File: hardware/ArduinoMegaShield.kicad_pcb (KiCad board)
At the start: 2 copper layers, 30 parts, among them P1 CONN_01X02, P10 CONN_01X02, P11 CONN_01X02, P12 CONN_01X02, P13 CONN_01X02, P14 CONN_01X02, P15 CONN_01X02, P16 CONN_01X02, P2 CONN_01X02, P3 CONN_01X02, P4 CONN_01X02, P5 CONN_01X02, P6 CONN_01X02, P7 CONN_01X02, P8 CONN_01X02, P9 CONN_01X02

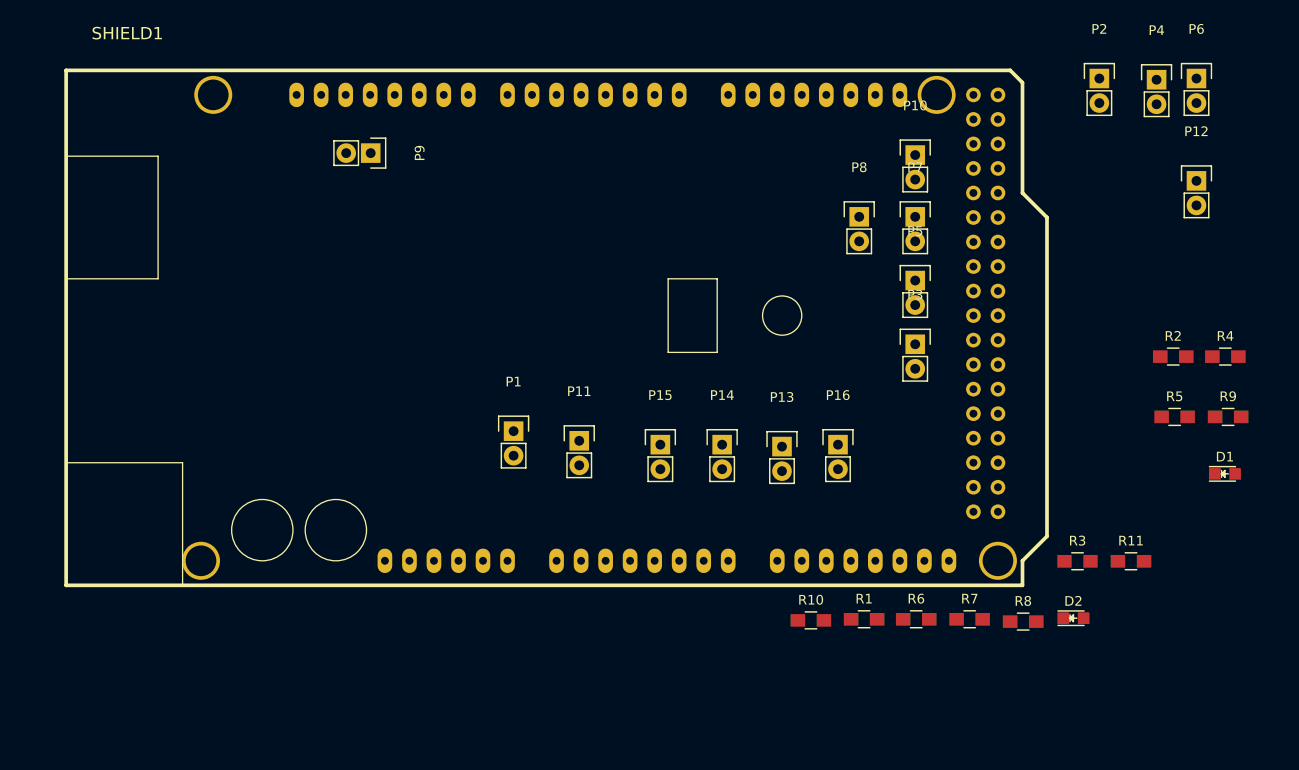
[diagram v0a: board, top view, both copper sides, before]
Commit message: changed terminal connectors from dupont to 200 mil screw terminals
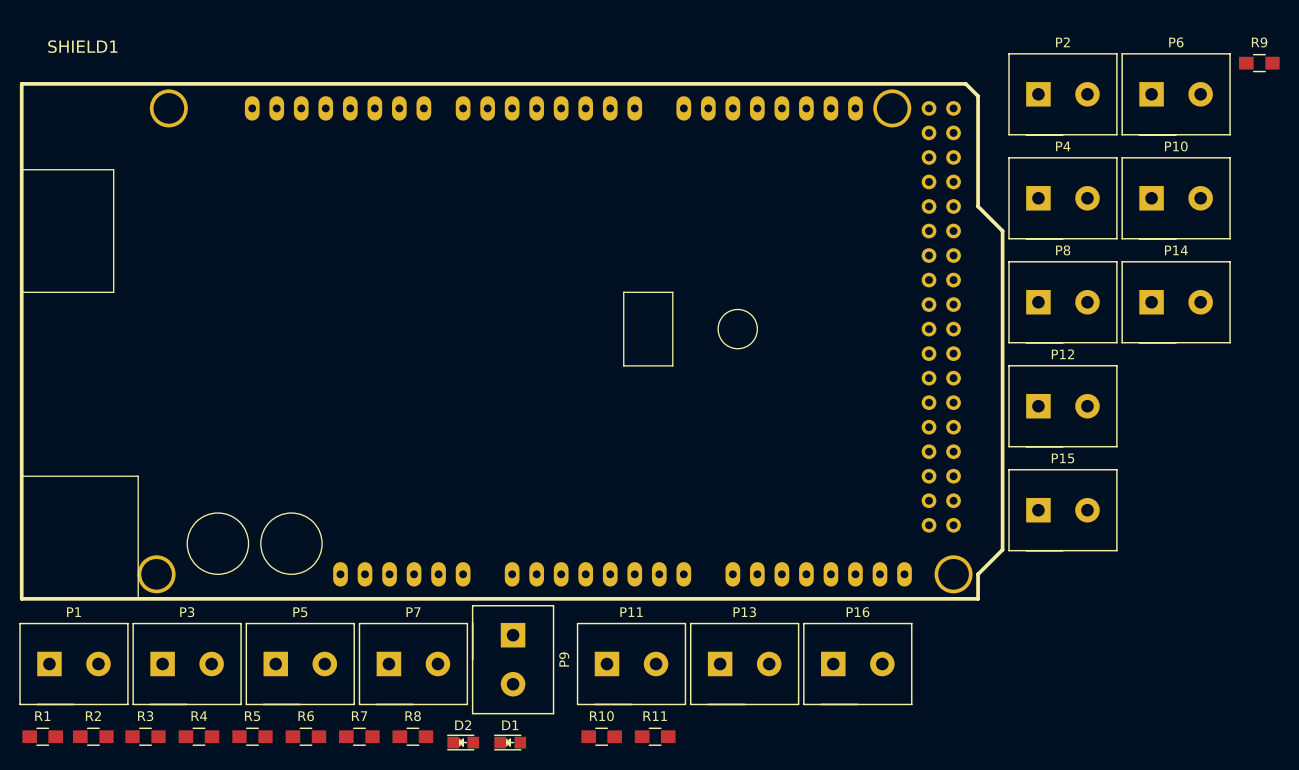
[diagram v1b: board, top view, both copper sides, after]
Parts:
- removed the P4 at (209.4, 72.0)
- added P2: CONN_01X02, 6axis:Terminal_Block_200_mil, F.Cu at (199.7, 73.5)
- P1, P10, P11, P12, P13, P14, P15, P16, P3, P5, P6, P7, P8, P9: footprint Pin_Headers:Pin_Header_Straight_1x02 -> 6axis:Terminal_Block_200_mil
- P4: renamed from P2; footprint Pin_Headers:Pin_Header_Straight_1x02 -> 6axis:Terminal_Block_200_mil
- moved R2 118.6 mm to (99.3, 140.1)
- moved R4 113.4 mm to (110.2, 140.1)
- moved R5 101.1 mm to (115.8, 140.1)
- moved R3 98.2 mm to (104.7, 140.1)
- moved R1 85.9 mm to (94.0, 140.1)
- moved P3 82.4 mm to (109.0, 132.5)
- moved D1 79.1 mm to (142.4, 140.7)
- moved P5 75.1 mm to (120.7, 132.5)
- moved P7 69.6 mm to (132.4, 132.5)
- moved D2 64.5 mm to (137.6, 140.7)
- moved R6 64.4 mm to (121.3, 140.1)
- moved R7 64.4 mm to (126.8, 140.1)
- moved R8 64.3 mm to (132.4, 140.1)
- moved P9 54.5 mm to (142.7, 132.1)
- moved R11 52.5 mm to (157.5, 140.1)
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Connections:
- P4 pad 1: /Z-Dir -> +5V
- P4 pad 2: GND -> /~ENABLE

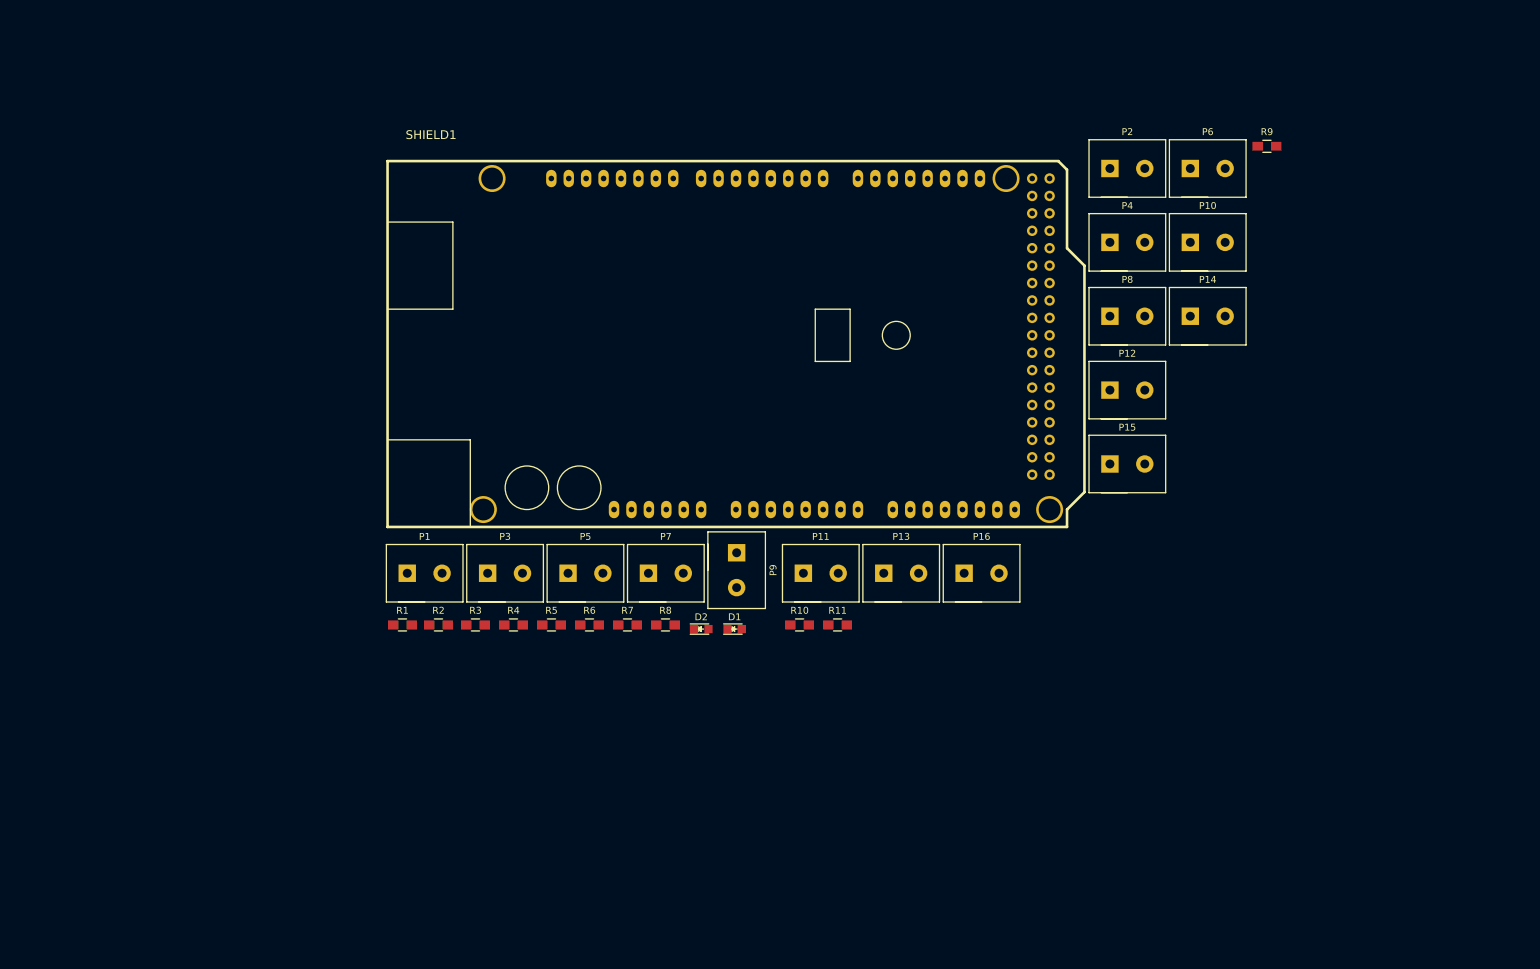
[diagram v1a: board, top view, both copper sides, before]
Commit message: added footprints for caps and motor drivers
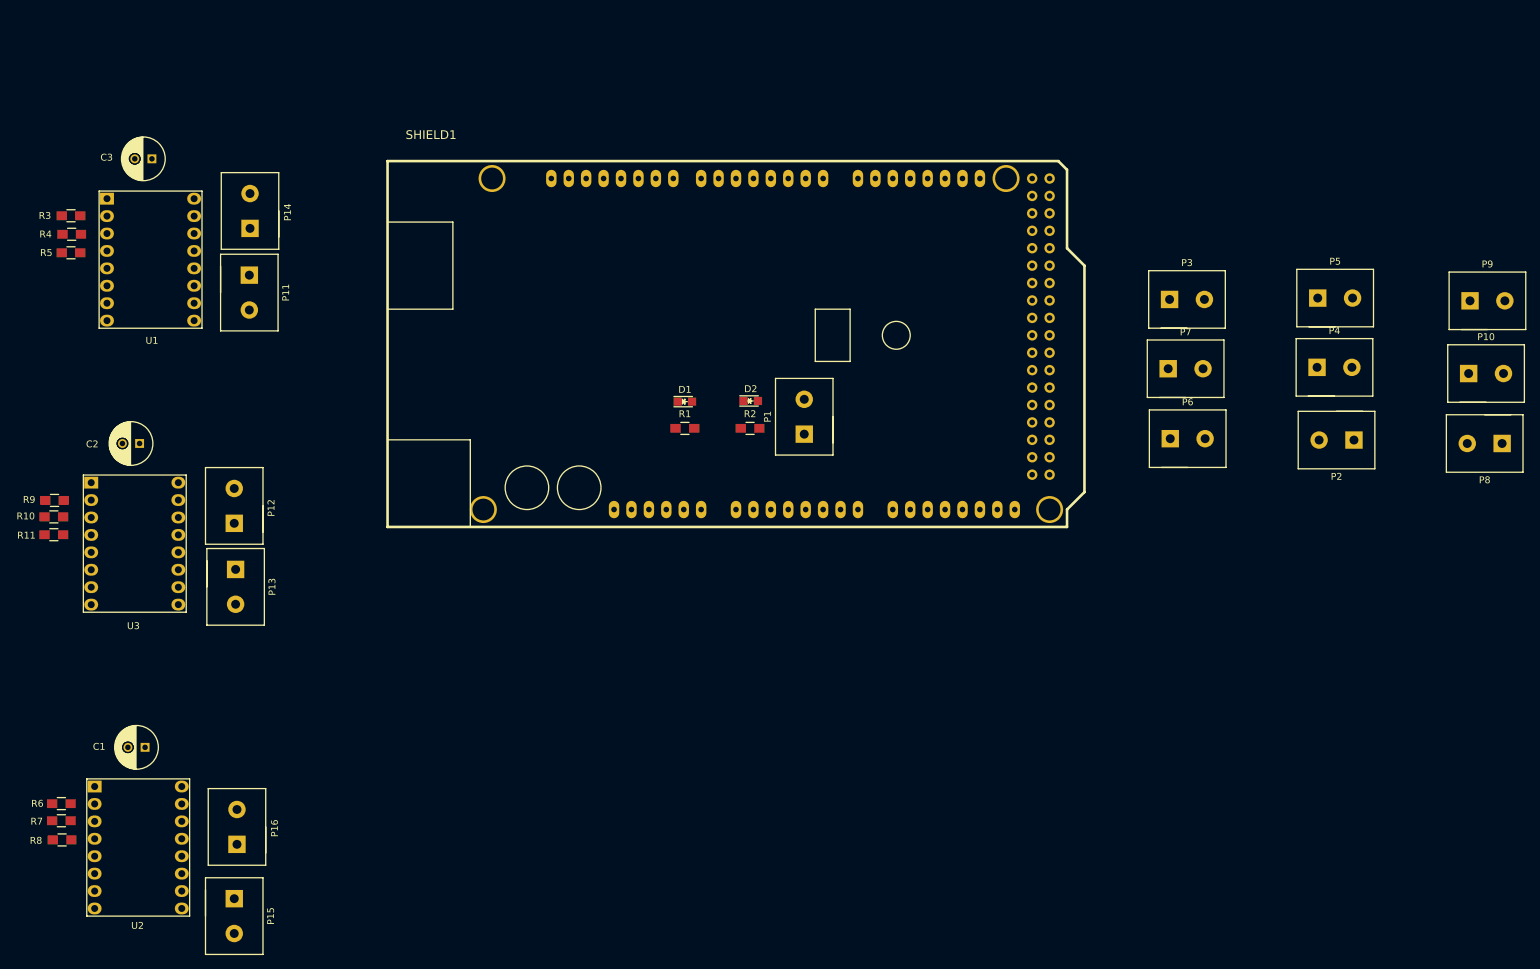
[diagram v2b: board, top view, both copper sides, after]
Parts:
- added C1: 100u, Capacitors_THT:C_Radial_D6.3_L11.2_P2.5, F.Cu at (56.5, 157.9)
- added C2: 100u, Capacitors_THT:C_Radial_D6.3_L11.2_P2.5, F.Cu at (55.7, 113.6)
- added C3: 100u, Capacitors_THT:C_Radial_D6.3_L11.2_P2.5, F.Cu at (57.5, 72.1)
- added U1: A4988, 6axis:A4988, F.Cu at (57.3, 86.8)
- added U2: A4988, 6axis:A4988, F.Cu at (55.5, 172.5)
- added U3: A4988, 6axis:A4988, F.Cu at (55.0, 128.2)
- moved R9 184.1 mm to (43.3, 121.9), turned to 180 degrees
- moved P15 145.9 mm to (69.5, 182.5), turned to 270 degrees
- moved P14 140.5 mm to (71.8, 79.7), turned to 90 degrees
- moved P12 131.3 mm to (69.5, 122.7), turned to 90 degrees
- moved P5 116.4 mm to (230.0, 92.4)
- moved P9 116.3 mm to (252.2, 92.8), turned to 0 degrees
- moved R11 115.0 mm to (43.2, 126.9), turned to 180 degrees
- moved P16 114.7 mm to (69.9, 169.5), turned to 90 degrees
- moved R10 109.9 mm to (43.2, 124.3), turned to 180 degrees
- moved P3 107.1 mm to (208.4, 92.6)
- moved P13 97.1 mm to (69.7, 134.5), turned to 270 degrees
- moved R8 93.4 mm to (44.4, 171.4), turned to 180 degrees
- moved P11 92.8 mm to (71.7, 91.6), turned to 270 degrees
- moved R5 88.6 mm to (45.7, 85.8), turned to 180 degrees
- moved R7 87.3 mm to (44.3, 168.6), turned to 180 degrees
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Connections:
- P11 pad 1: (no net) -> /A1A
- P11 pad 2: (no net) -> /A1B
- P12 pad 1: (no net) -> /C2A
- P12 pad 2: (no net) -> /C2B
- P13 pad 1: (no net) -> /C1A
- P13 pad 2: (no net) -> /C1B
- P14 pad 1: (no net) -> /A2A
- P14 pad 2: (no net) -> /A2B
- P15 pad 1: (no net) -> /B1A
- P15 pad 2: (no net) -> /B1B
- P16 pad 1: (no net) -> /B2A
- P16 pad 2: (no net) -> /B2B
- R10 pad 1: (no net) -> Net-(R10-Pad1)
- R11 pad 1: (no net) -> Net-(R11-Pad1)
- R3 pad 1: (no net) -> Net-(R3-Pad1)
- R4 pad 1: (no net) -> Net-(R4-Pad1)
- R5 pad 1: (no net) -> Net-(R5-Pad1)
- R6 pad 1: (no net) -> Net-(R6-Pad1)
- R7 pad 1: (no net) -> Net-(R7-Pad1)
- R8 pad 1: (no net) -> Net-(R8-Pad1)
- R9 pad 1: (no net) -> Net-(R9-Pad1)
- SHIELD1 pad 27: (no net) -> /A-Step
- SHIELD1 pad 28: (no net) -> /B-Step
- SHIELD1 pad 29: (no net) -> /C-Step
- SHIELD1 pad 33: (no net) -> /A-Dir
- SHIELD1 pad 34: (no net) -> /B-Dir
- SHIELD1 pad 35: (no net) -> /C-Dir

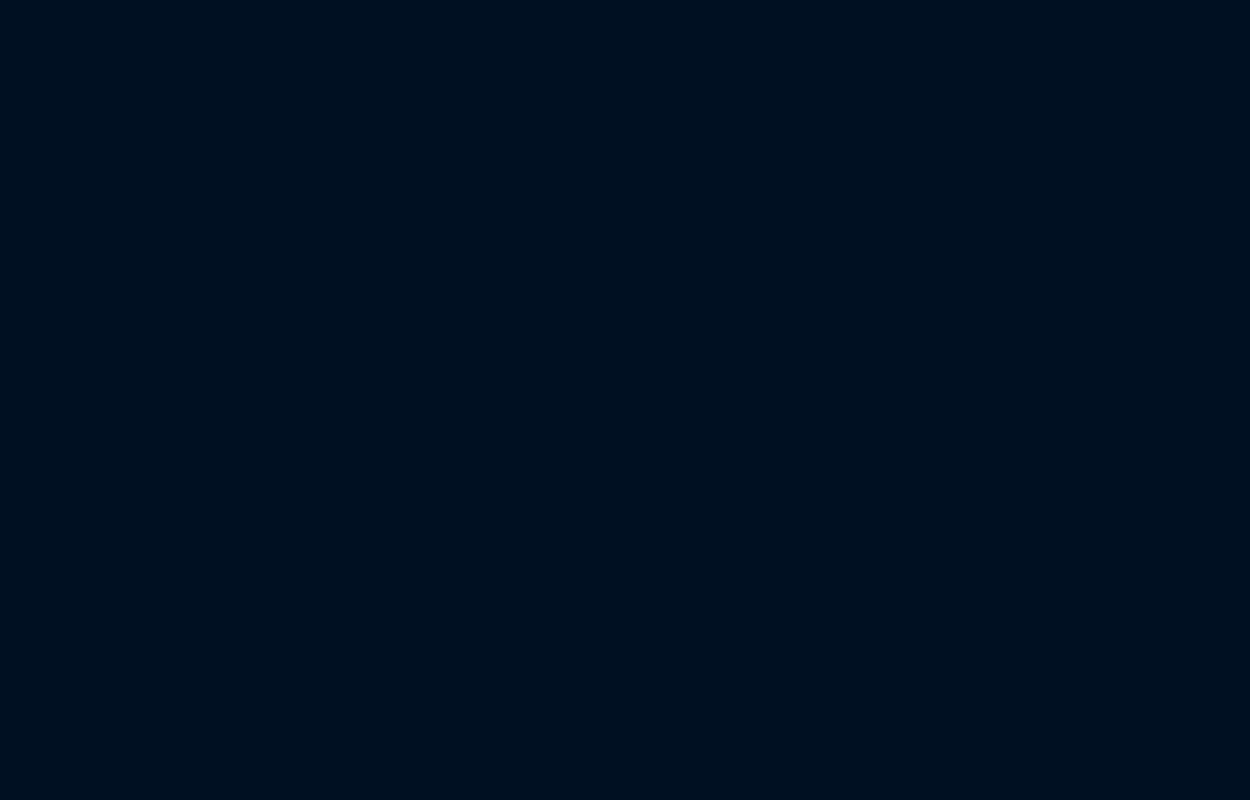
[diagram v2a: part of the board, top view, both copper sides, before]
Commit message: added terminal connections for limit switches
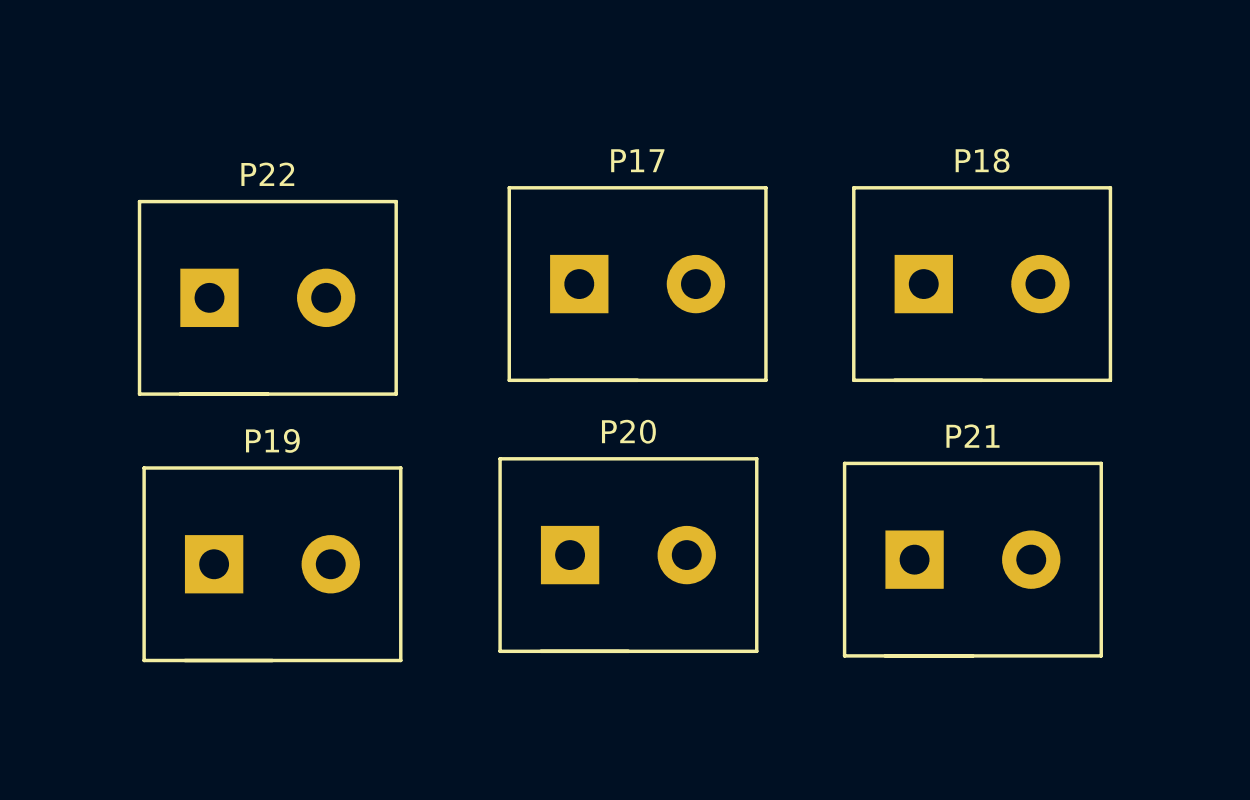
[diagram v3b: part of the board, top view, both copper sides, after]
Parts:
- added P17: CONN_01X02, 6axis:Terminal_Block_200_mil, F.Cu at (170.2, 146.4)
- added P18: CONN_01X02, 6axis:Terminal_Block_200_mil, F.Cu at (185.2, 146.4)
- added P19: CONN_01X02, 6axis:Terminal_Block_200_mil, F.Cu at (154.3, 158.6)
- added P20: CONN_01X02, 6axis:Terminal_Block_200_mil, F.Cu at (169.8, 158.2)
- added P21: CONN_01X02, 6axis:Terminal_Block_200_mil, F.Cu at (184.8, 158.4)
- added P22: CONN_01X02, 6axis:Terminal_Block_200_mil, F.Cu at (154.1, 147.0)
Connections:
- D1 pad 1: (no net) -> GND
- D2 pad 1: (no net) -> GND
- SHIELD1 pad 10: (no net) -> /X_LIMIT
- SHIELD1 pad 11: (no net) -> /Y_LIMIT
- SHIELD1 pad 12: (no net) -> /Z_LIMIT
- SHIELD1 pad 51: (no net) -> /C_LIMIT
- SHIELD1 pad 52: (no net) -> /B_LIMIT
- SHIELD1 pad 53: (no net) -> /A_LIMIT
